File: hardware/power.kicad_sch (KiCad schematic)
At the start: 36 parts, among them J1 USB4110-GF-A, J2 B2B-PH-K-S, J3 PRPC001DAAN-RC, J4 PRPC001DAAN-RC, J5 PRPC001DAAN-RC, Q1 IRLML2246TRPBF, Q2 IRLML2246TRPBF, U1 USBLC6-2SC6, U2 MCP73811T-420I-OT, U3 TPS61023DRLR

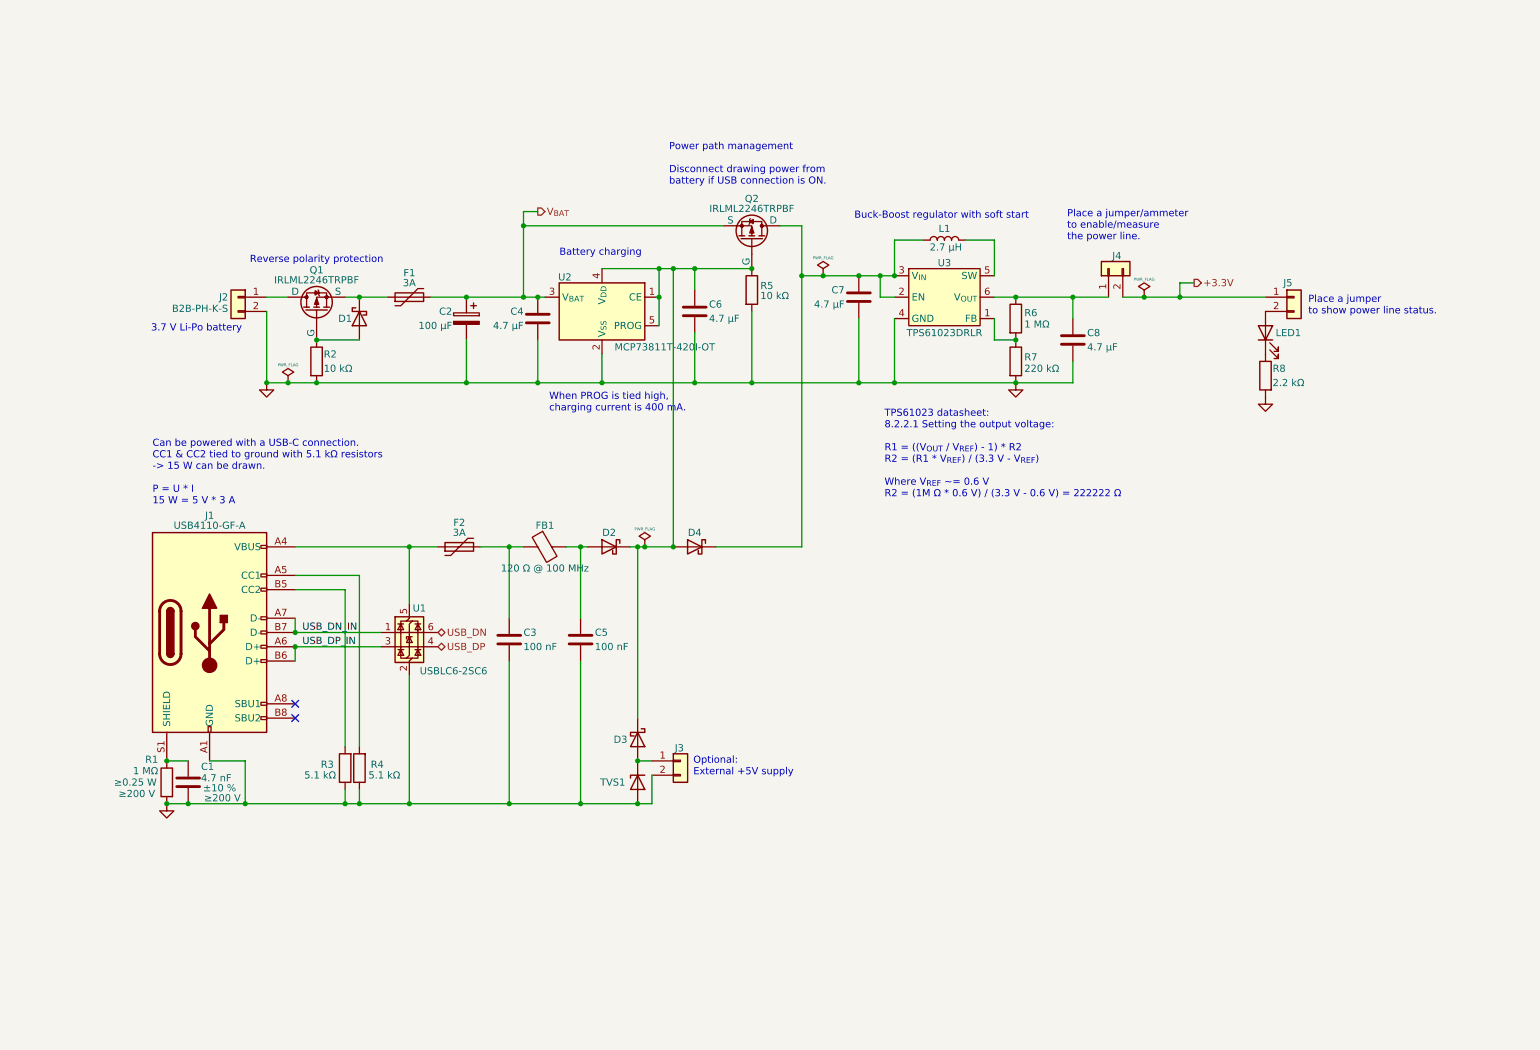
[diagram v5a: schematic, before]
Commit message: HW: Add battery protection
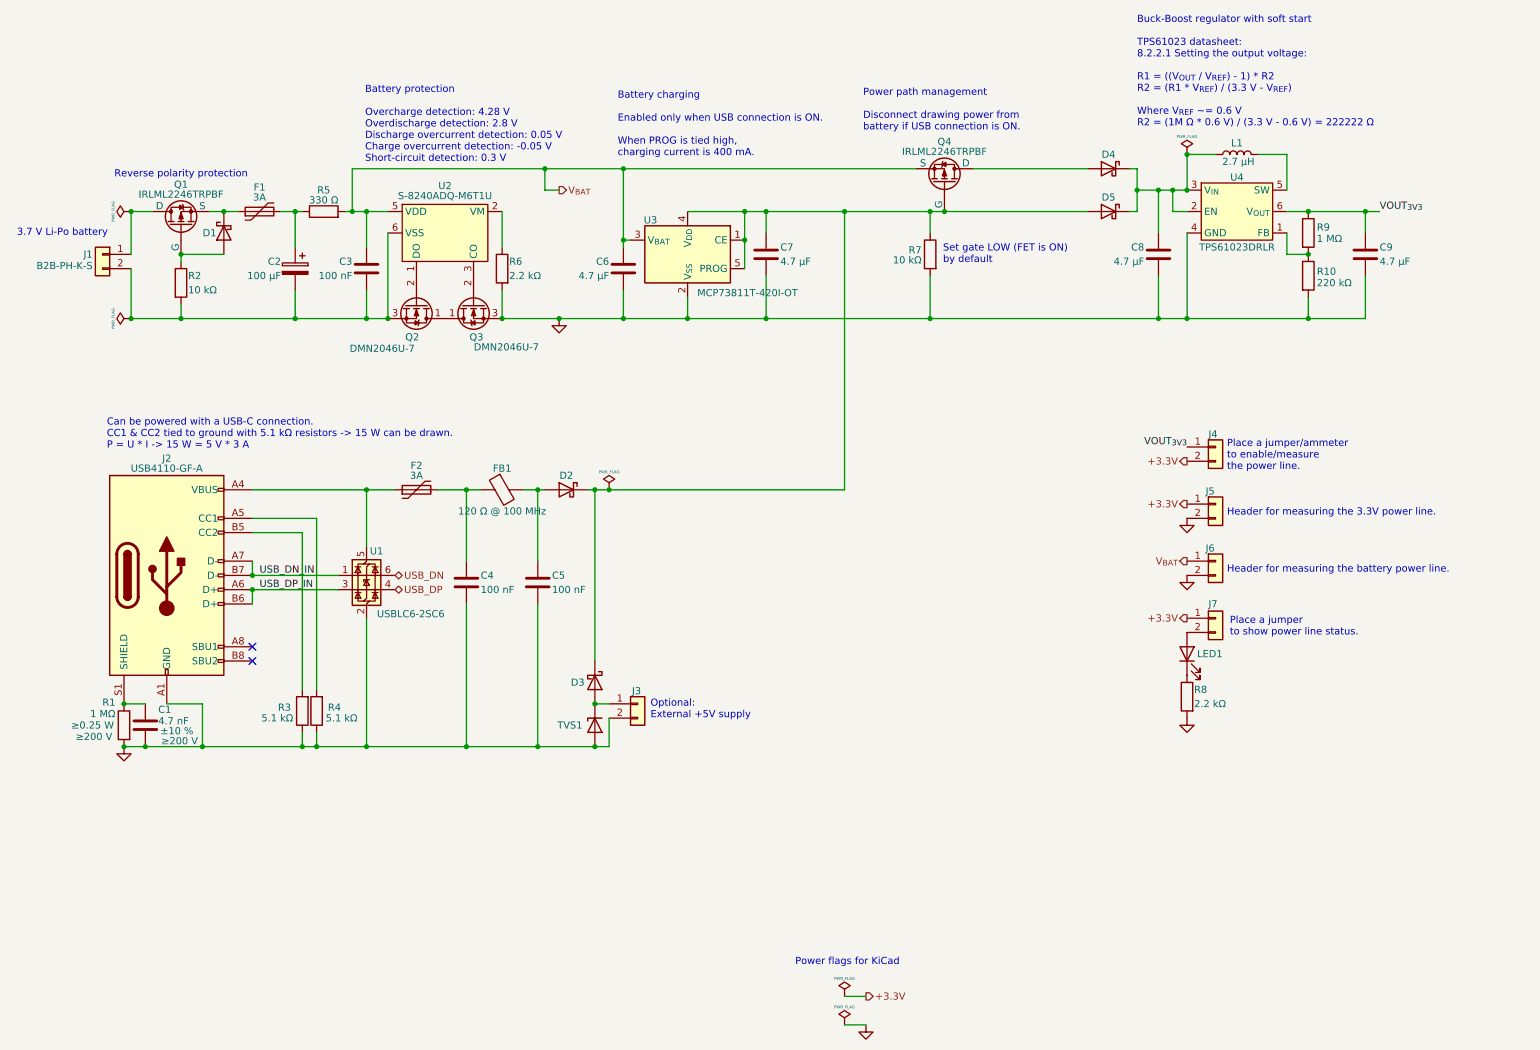
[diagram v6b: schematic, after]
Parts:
- added C3: 100 nF, Capacitor_SMD:C_0402_1005Metric_Pad0.74x0.62mm_HandSolder, symbol Device:C
- added D4: CDBA140LL-HF, Diode_SMD:D_SMA_Handsoldering, symbol Device:D_Schottky
- added J5, J6: PRPC001DAAN-RC, Connector_PinHeader_2.54mm:PinHeader_1x02_P2.54mm_Vertical, symbol Connector_Generic:Conn_01x02
- added Q2, Q3: DMN2046U-7, Package_TO_SOT_SMD:SC-59_Handsoldering, symbol Device:Q_NMOS_DGS
- added R6: 2.2 kΩ, Resistor_SMD:R_0402_1005Metric_Pad0.72x0.64mm_HandSolder, symbol Device:R
- added R7: 10 kΩ, Resistor_SMD:R_0402_1005Metric_Pad0.72x0.64mm_HandSolder, symbol Device:R
- added U2: S-8240ADQ-M6T1U, Package_TO_SOT_SMD:SOT-23-6, symbol S-8240A:S-8240ADQ-M6T1U
- R5: value 10 kΩ -> 330 Ω; footprint Resistor_SMD:R_0402_1005Metric_Pad0.72x0.64mm_HandSolder -> Resistor_SMD:R_0805_2012Metric_Pad1.20x1.40mm_HandSolder; Digi-Key Part Number 732-560112110020CT-ND -> 732-560112120017CT-ND; Manufacturer Part Number 560112110020 -> 560112120017
- renumbered C3 to C4, C4 to C6, C6 to C7, C7 to C8, C8 to C9, D4 to D5, J2 to J1, J1 to J2, J5 to J7, Q2 to Q4, R7 to R10, R6 to R9, U2 to U3, U3 to U4
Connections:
- net +3.3V: now also J5.1 (Pin_1)
- net GND: now also J5.2 (Pin_2), J6.2 (Pin_2), Q3.3 (S), R6.2, R7.2; no longer C2.2, J1.2 (Pin_2), R2.2, R5.2
- net V_{BAT}: now also R5.2, C3.1, J6.1 (Pin_1), U2.5 (VDD); no longer C2.1, F1.2
- net at C7.1, D2.1 (K), D3.1 (K)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: now also R7.1; no longer R5.1
- net VOUT_{3V3}: now reaches C9.1, J4.1 (Pin_1), R9.1, U4.6 (V_{OUT})
- net at C8.1, D5.1 (K), L1.1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: now also D4.1 (K); no longer Q4.1 (D)
- new net: C2.2, C3.2, J1.2 (Pin_2), Q2.3 (S), R2.2, U2.6 (VSS)
- new net: Q2.1 (D), Q3.1 (D)
- new net: Q3.2 (G), U2.3 (CO)
- new net: C2.1, F1.2, R5.1
- new net: R6.1, U2.2 (VM)
- new net: Q2.2 (G), U2.1 (DO)
- new net: D4.2 (A), Q4.1 (D)
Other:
- note added: "Battery charging Enabled only when USB connection is ON. When PROG is tied high, charging current is 400 mA."
- note added: "Battery protection Overcharge detection: 4.28 V Overdischarge detection: 2.8 V Discharge overcurrent detection: 0.05 V Charge overcurrent detection: -0.05 V Short-circuit detection: 0.3 V"
- note added: "Buck-Boost regulator with soft start TPS61023 datasheet: 8.2.2.1 Setting the output voltage: R1 = ((V_{OUT} / V_{REF}) - 1) * R2 R2 = (R1 * V_{REF}) / (3.3 V - V_{REF}) Where V_{REF} ~= 0.6 V R2 = (1M Ω * 0.6 V) / (3.3 V - 0.6 V) = 222222 Ω"
- note added: "Can be powered with a USB-C connection. CC1 & CC2 tied to ground with 5.1 kΩ resistors -> 15 W can be drawn. P = U * I -> 15 W = 5 V * 3 A"
- note added: "Header for measuring the 3.3V power line."
- note added: "Header for measuring the battery power line."
- note added: "Power flags for KiCad"
- note added: "Set gate LOW (FET is ON) by default"
- note removed: "Battery charging"
- note removed: "Buck-Boost regulator with soft start"
- note removed: "Can be powered with a USB-C connection. CC1 & CC2 tied to ground with 5.1 kΩ resistors -> 15 W can be drawn. P = U * I 15 W = 5 V * 3 A"
- note removed: "TPS61023 datasheet: 8.2.2.1 Setting the output voltage: R1 = ((V_{OUT} / V_{REF}) - 1) * R2 R2 = (R1 * V_{REF}) / (3.3 V - V_{REF}) Where V_{REF} ~= 0.6 V R2 = (1M Ω * 0.6 V) / (3.3 V - 0.6 V) = 222222 Ω"
- note removed: "When PROG is tied high, charging current is 400 mA."
- moved on the sheet: C1, C2, C4, C5, C6, C7, C8, C9, D1, D2, D3, D5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
